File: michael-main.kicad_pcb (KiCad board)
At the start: 4 copper layers, 98 x 119.8 mm, 177 parts, among them J1 Conn_01x03_Pin, J14 Conn_01x02_Pin, J15 Conn_01x02_Pin, J17 Conn_01x03_Pin, J18 Conn_01x05_Pin, J19 Conn_01x03_Pin, J21 Conn_01x05_Pin, J22 Conn_01x02_Pin, J25 Conn_01x09_Socket, J27 Conn_01x07_Socket, J28 XT30PW_2_2_-M.G.B, J29 XT30PW_2_2_-M.G.B, J3 Conn_01x03_Pin, J30 XT30PW_2_2_-M.G.B, J31 XT30PW_2_2_-M.G.B, J4 Conn_01x05_Pin, J5 Conn_01x05_Pin, J7 Conn_01x03_Pin, J8 USB_B_Mini, J9 Conn_01x05_Pin, Q1 BSC340N08NS3G, Q2 BSC340N08NS3G, Q3 BSC340N08NS3G, Q4 BSC340N08NS3G, U1 STM32F446RETx, U11 LMR14050SDDAR, U12 LMR14050SDDAR, U13 STM32F446RETx, U14 LM1084-5.0, U16 LM1084-3.3, U17 SN65HVD230, U18 SN65HVD230, U2 SN65HVD230, U3 STM32F446RETx, U4 SN65HVD230, U5 USBLC6-4SC6, U6 STM32F446RETx, U8 LTC7000EMSE-1_TRPBF, U9 STM32F446RETx, Y1 Crystal, Y2 8Mhz, Y3 Crystal, Y4 Crystal, Y5 Crystal

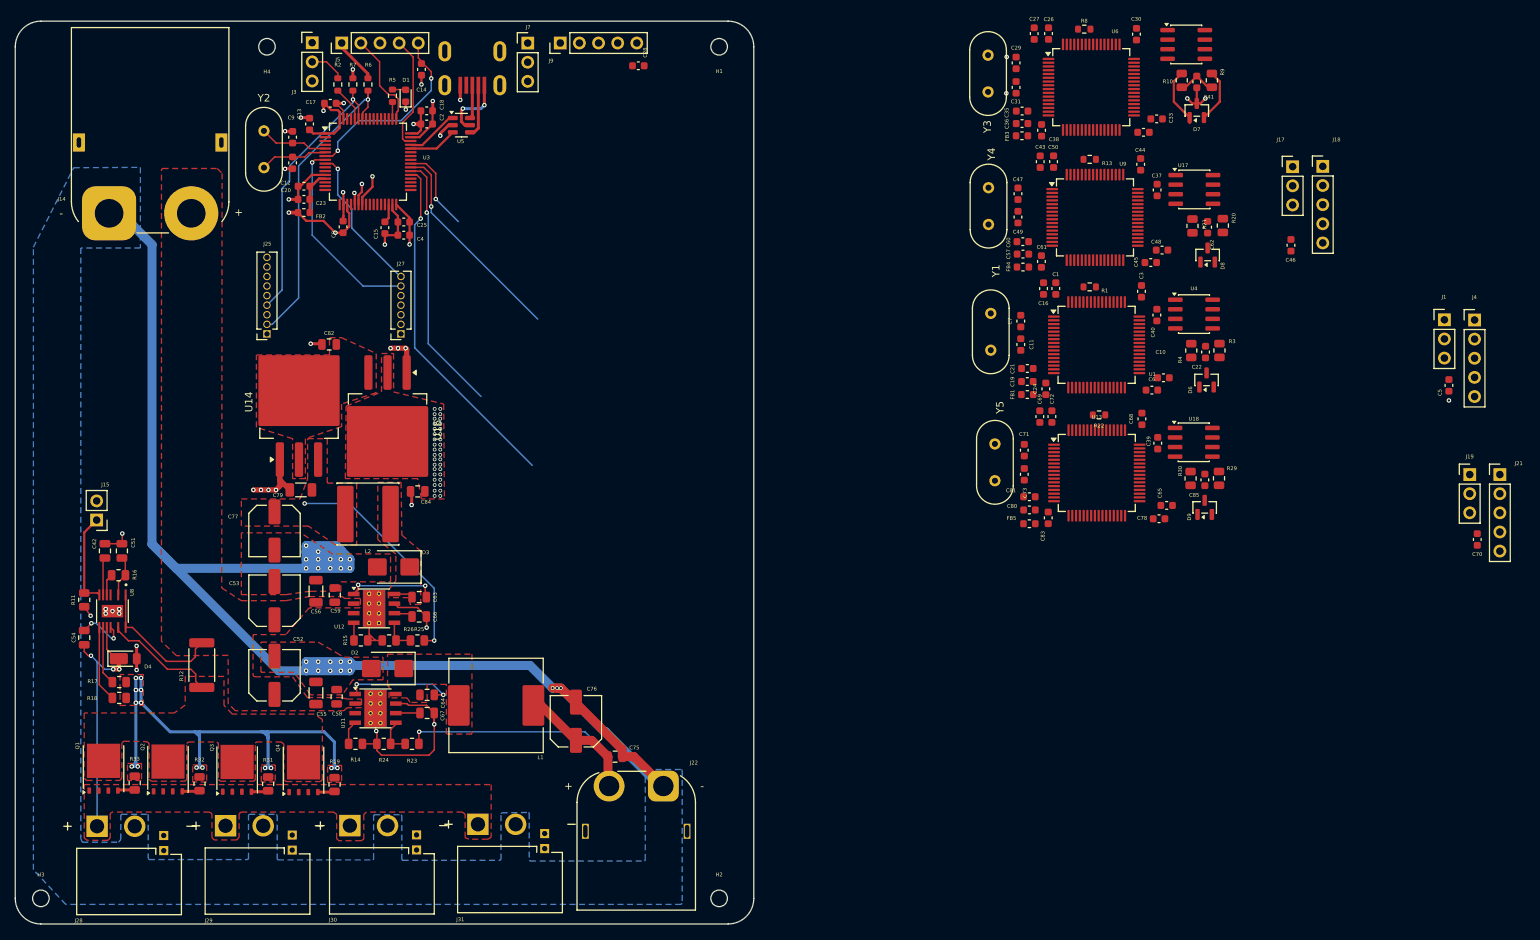
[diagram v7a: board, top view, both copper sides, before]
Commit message: updated routing for shorter power trace
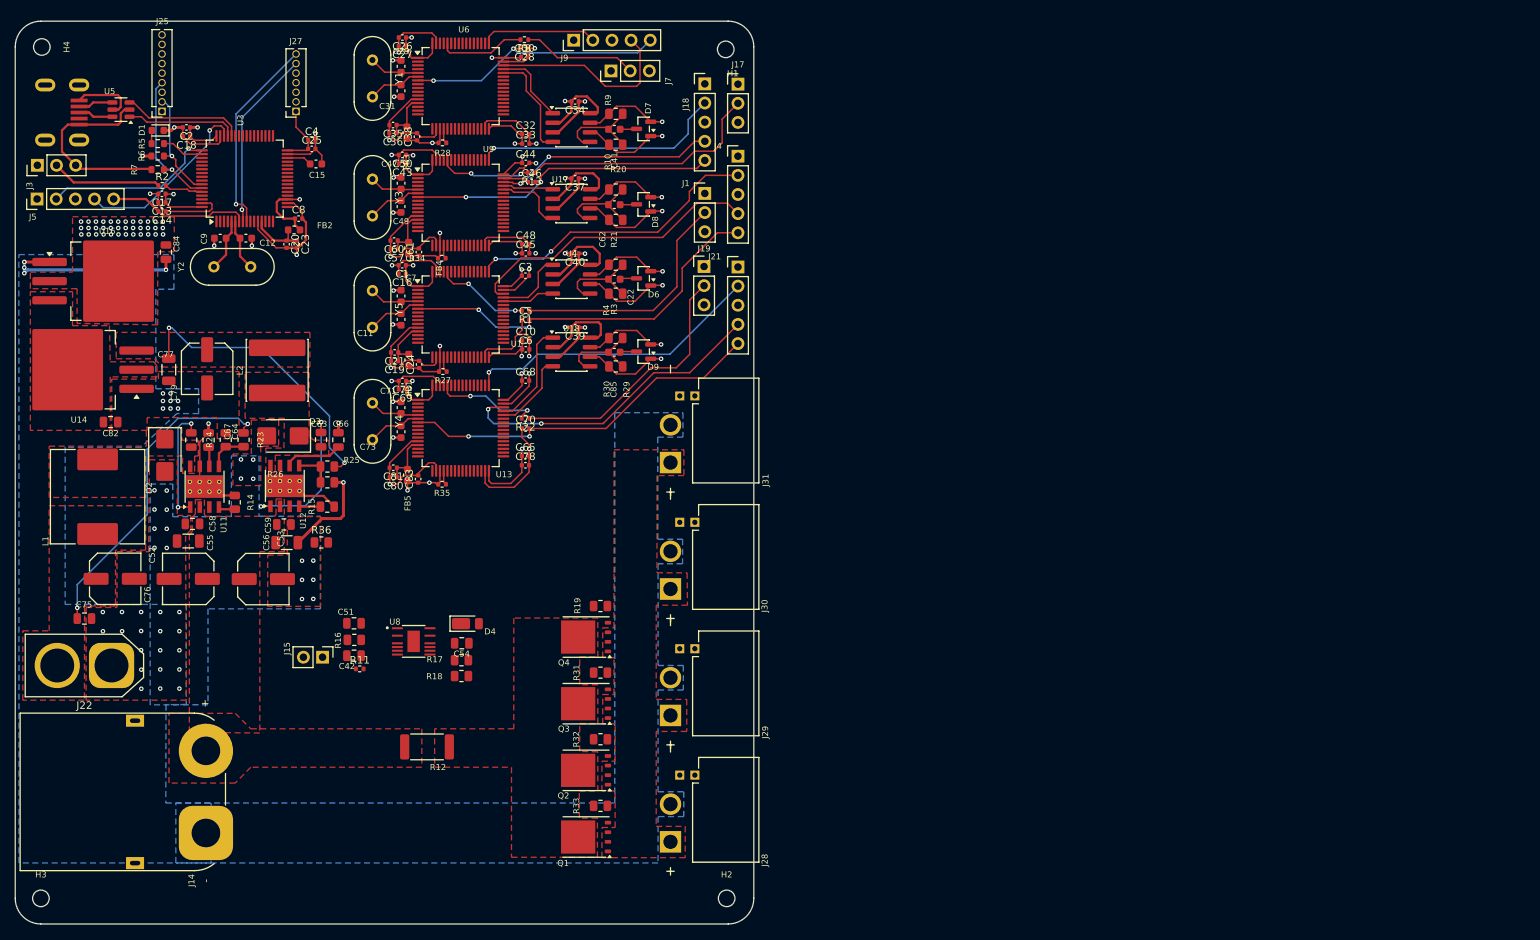
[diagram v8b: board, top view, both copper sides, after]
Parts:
- added C34: 0.1uF, Capacitor_SMD:C_0402_1005Metric, F.Cu at (110.9, 59.2)
- added R27: 47k, Resistor_SMD:R_0402_1005Metric, F.Cu at (93.3, 95.1)
- added R28: 47k, Resistor_SMD:R_0402_1005Metric, F.Cu at (93.3, 64.8)
- added R34: 47k, Resistor_SMD:R_0402_1005Metric, F.Cu at (93.2, 80.1)
- added R35: 47k, Resistor_SMD:R_0402_1005Metric, F.Cu at (93.2, 110.0)
- added R36: 0, Resistor_SMD:R_0805_2012Metric, F.Cu at (77.2, 117.8)
- C1, C10, C13, C14, C16, C17, C18, C19, C2, C20, C21, C23, C24, C25, C26, C27, C28, C3, C30, C32, C33, C35, C36, C37, C38, C39, C4, C40, C43, C44, C45, C46, C48, C5, C50, C57, C6, C60, C61, C65, C68, C69, C70, C72, C78, C8, C80, C81, C83: footprint Capacitor_SMD:C_0603_1608Metric -> Capacitor_SMD:C_0402_1005Metric
- J22: footprint Connector_AMASS:AMASS_XT60PW-M_1x02_P7.20mm_Horizontal -> Connector_AMASS:AMASS_XT60-M_1x02_P7.20mm_Vertical
- R1, R13, R2, R22, R8: footprint Resistor_SMD:R_0603_1608Metric -> Resistor_SMD:R_0402_1005Metric
- R11: footprint Resistor_SMD:R_0805_2012Metric -> Resistor_SMD:R_0402_1005Metric
- Y1, Y3, Y4, Y5: value Crystal -> 8Mhz
- moved C70 127.1 mm to (104.3, 102.7), turned to 0 degrees
- moved C5 122.8 mm to (104.3, 88.2), turned to 0 degrees
- moved J19 105.3 mm to (128.0, 81.2)
- moved J21 104.8 mm to (132.5, 81.2)
- moved C46 101.1 mm to (105.1, 70.0), turned to 0 degrees
- moved J4 100.1 mm to (132.5, 66.5)
- moved J1 99.6 mm to (128.1, 71.5)
- moved Y1 88.7 mm to (84.0, 53.8)
- moved C1 86.8 mm to (87.9, 81.0), turned to 180 degrees
- moved Y4 86.6 mm to (84.0, 99.3)
- moved C50 86.4 mm to (88.0, 66.3), turned to 180 degrees
- moved C72 86.3 mm to (88.0, 96.3), turned to 180 degrees
- moved C26 85.7 mm to (88.0, 50.8), turned to 180 degrees
- moved C65 85.3 mm to (104.3, 106.3)
- moved C16 85.1 mm to (87.9, 82.1), turned to 180 degrees
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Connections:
- net Net-(U11-FB) renamed /FB15
- net Net-(U12-FB) renamed /FB6
- C52 pad 2: GND -> GNDPWR
- C53 pad 2: GND -> GNDPWR
- C55 pad 2: GND -> GNDPWR
- C56 pad 2: GND -> GNDPWR
- C58 pad 2: GND -> GNDPWR
- C59 pad 2: GND -> GNDPWR
- C75 pad 2: GND -> GNDPWR
- C76 pad 2: GND -> GNDPWR
- C77 pad 2: GND -> GNDPWR
- C79 pad 2: GND -> GNDPWR
- C82 pad 2: GND -> GNDPWR
- C84 pad 2: GND -> GNDPWR
- D2 pad 2: GND -> GNDPWR
- D3 pad 2: GND -> GNDPWR
- J14 pad 1: GND -> GNDPWR
- J15 pad 2: GND -> +3.3V
- J22 pad 1: GND -> GNDPWR
- J28 pad N: GND -> GNDPWR
- J29 pad N: GND -> GNDPWR
- J30 pad N: GND -> GNDPWR
- J30 pad S1: /CANH2 -> /CANH3
- J30 pad S2: /CANL2 -> /CANL3
- J31 pad N: GND -> GNDPWR
- J31 pad S1: /CANH3 -> /CANH2
- J31 pad S2: /CANL3 -> /CANL2
- R11 pad 2: +3.3V -> GND
- R24 pad 2: GND -> GNDPWR
- R26 pad 2: GND -> GNDPWR
- U14 pad 1: GND -> GNDPWR
- U16 pad 1: GND -> GNDPWR
- U8 pad 8: Net-(J15-Pin_1) -> Net-(J2-Pin_2)
- Y1 pad 1: Net-(U1-PH0) -> Net-(U6-PH0)
- Y1 pad 2: Net-(U1-PH1) -> Net-(U6-PH1)
- Y3 pad 1: Net-(U6-PH0) -> Net-(U9-PH0)
- Y3 pad 2: Net-(U6-PH1) -> Net-(U9-PH1)
- Y4 pad 1: Net-(U9-PH0) -> Net-(U13-PH0)
- Y4 pad 2: Net-(U9-PH1) -> Net-(U13-PH1)
- Y5 pad 1: Net-(U13-PH0) -> Net-(U1-PH0)
- Y5 pad 2: Net-(U13-PH1) -> Net-(U1-PH1)
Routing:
- net +3.3V: track 93.6 -> 169.2 mm, vias 42 -> 61
- net Net-(R17-Pad2): track 66.5 -> 0.00 mm, vias 14 -> 0
- net /NRST1: track 0.00 -> 51.0 mm, vias 1 -> 2
- net /NRST4: track 0.00 -> 49.0 mm, vias 0 -> 2
- net /CS3: track 46.4 -> 1.90 mm, vias 1 -> 0
- net /TMS4: track 0.00 -> 42.2 mm, vias 0 -> 2
- net /NRST3: track 0.00 -> 41.3 mm, vias 0 -> 2
- net /CANH3: track 27.8 -> 67.7 mm, vias 0 -> 1
- net /TCK4: track 0.00 -> 39.5 mm, vias 0 -> 1
- net /TCK1: track 0.00 -> 39.5 mm, vias 0 -> 2
- net /TMS1: track 0.00 -> 39.4 mm
- net /CANL3: track 26.3 -> 65.0 mm, vias 0 -> 1
- net GNDPWR: track 0.00 -> 38.4 mm, vias 0 -> 50
- net +24V: track 35.3 -> 0.00 mm, vias 3 -> 0
- net Net-(J19-Pin_2): track 0.00 -> 34.7 mm
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- added copper zone on F.Cu, net +15V
- added copper zone on B.Cu, net GNDPWR
- added copper zone on F.Cu, net GNDPWR
- removed copper zone on B.Cu, net GND
- removed copper zone on F.Cu, net GND
- removed copper zone on F.Cu, net Net-(R17-Pad2)
